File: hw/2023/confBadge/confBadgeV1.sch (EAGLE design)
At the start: 86 parts, among them J3 TYPE-C-31-M-12, Q1 8/16/20MHz, U1 ATMEGA328, U10 WS2812-2020, U11 WS2812-2020, U12 WS2812-2020, U13 WS2812-2020, U14 WS2812-2020, U15 WS2812-2020, U16 WS2812-2020, U17 WS2812-2020, U18 WS2812-2020, U19 WS2812-2020, U2 AP2112-3.3, U20 WS2812-2020, U21 WS2812-2020, U22 WS2812-2020, U3 WS2812-2020, U4 WS2812-2020, U5 PCM12SMTRPCM12SMTR_CNK, U6 24792479PCB_37P49X52P63_KEY, U7 CH340C, U8 SMF05CT1G, U9 WS2812-2020

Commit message: Updated schematic and layout for Conf-Badge
- adjusted for ATmega328PB
- change to USB-c
- switch sao and isp header to SMD
- moved sync-in and sync-out header for fit
- updated silkscreen for oled position
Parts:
- removed SV4: SAO, con-lstb:MA03-2
- removed SV5: ICSP, con-lstb:MA03-2
- added J1, J2: SSW-103-22-F-D-VS-K-TRCON3_SSW-D-DUMZ_HDR_SAI, SSW-103-22-F-D-VS-K-TR:SSW-103-22-F-D-VS-K-TRCON3_SSW-D-DUMZ_HDR_SAI
- added R16, R17, R18, R19, R8, R9: 10K, SparkFun:RESISTOR0603-RES
- added TP1, TP2: TPB1,27, testpad:TPB1,27
- R13, R14: value 1K -> 5.1K
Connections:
- new net PE0: TP2.TP, U1.GND@1
- new net PE1: TP1.TP, U1.VCC@2
- net 3.3V: now also J1.6, J2.1, R16.2, R17.2, R18.2, R19.2, R8.2, R9.2; no longer SV4.2, SV5.2, U1.VCC@2
- net BTN_A: now also R19.1
- net BTN_B: now also R18.1
- net BTN_D: now also R9.1
- net BTN_L: now also R8.1
- net BTN_R: now also R17.1
- net BTN_U: now also R16.1
- net DBG_LED: now also J1.3; no longer SV5.3
- net GND: now also J1.2, J2.2; no longer SV4.1, SV5.6, U1.GND@1
- net RESET: now also J1.1; no longer SV5.5
- net SAO_IO1: now also J1.4, J2.5; no longer SV4.6, SV5.4
- net SAO_IO2: now also J1.5, J2.6; no longer SV4.5, SV5.1
- net SCL: now also J2.4; no longer SV4.3
- net SDA: now also J2.3; no longer SV4.4
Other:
- note added: "8MHZ"
- note added: "Digikey: 2057-PH1RB-05-UA-ND Manuf: PH1RB-05-UA"
- note added: "Digikey: S5441-ND Manuf: PPTC051LGBN"
- note added: "ISP CONNECTOR"
- note added: "RESET GND SCK MOSI MISO 3V3"
- note added: "SAO CONNECTOR"
- note added: "Switch to Atmega328PB (for UID)"
- note removed: "MISO SCK RESET"
- note removed: "VCC MOSI GND"
- moved on the sheet: C1, C2, D2, Q1, R2, R6, S1, U1

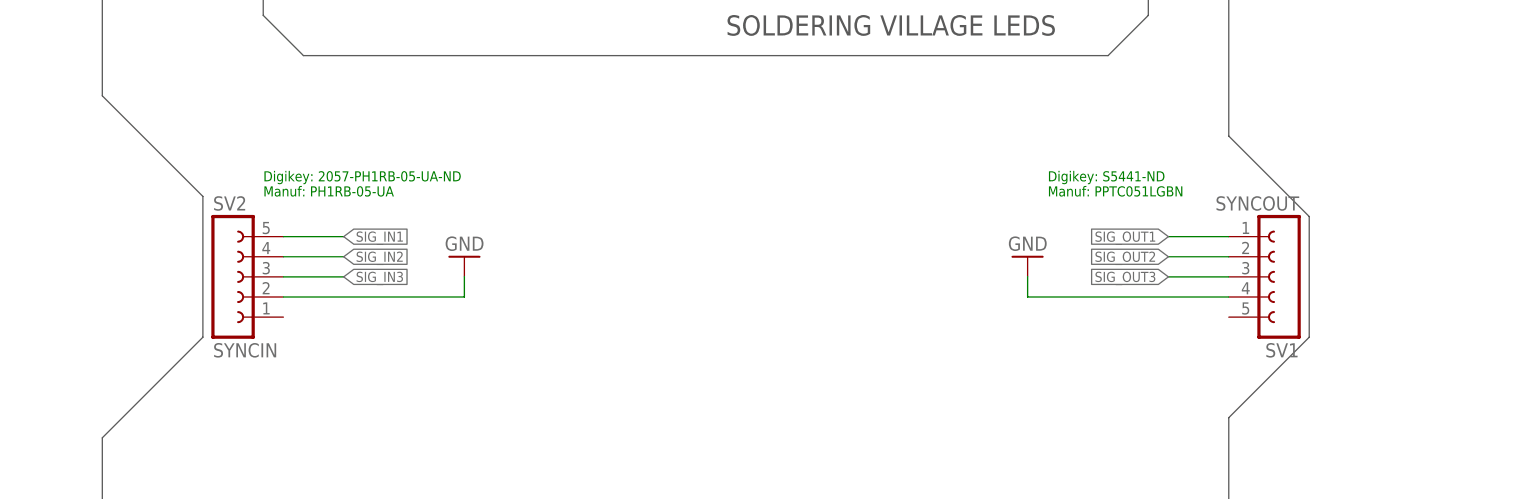
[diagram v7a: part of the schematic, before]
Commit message: added bottom pick-place file for rizome quote
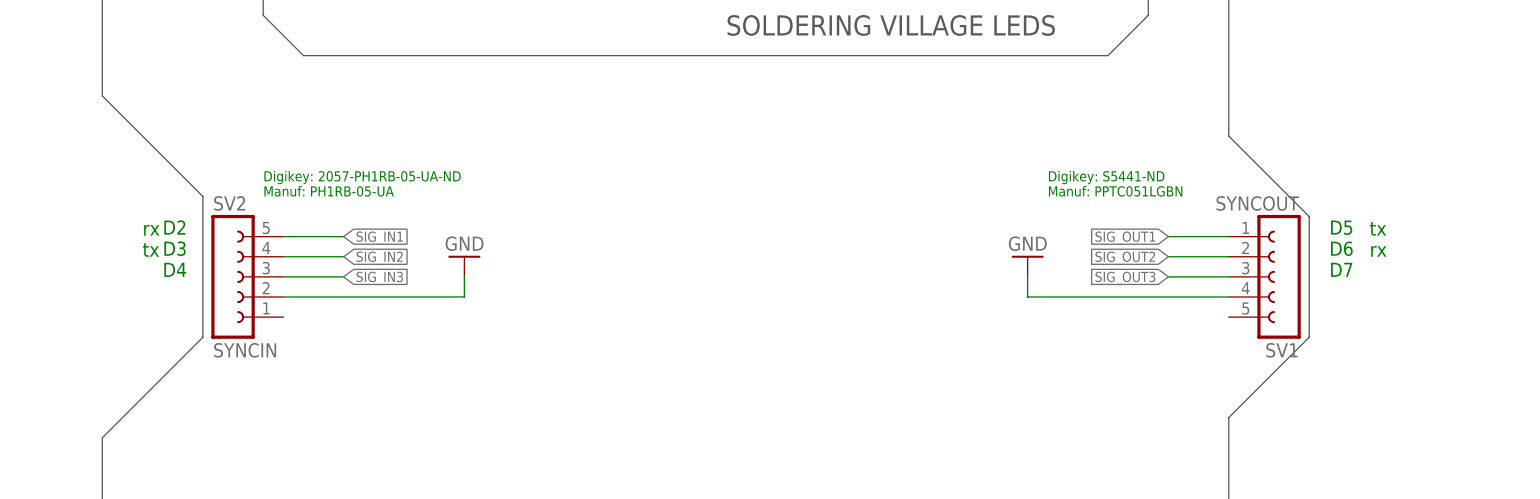
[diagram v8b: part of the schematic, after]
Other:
- note added: "D2 D3 D4"
- note added: "D5 D6 D7"
- note added: "rx tx"
- note added: "tx rx"
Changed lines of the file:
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@@
 (for UID)</text>
 <text x="81.28" y="83.82" size="2.54" layer="91">8MHZ</text>
+<text x="584.2" y="86.36" size="1.778" layer="91">D2
+D3
+D4</text>
+<text x="731.52" y="86.36" size="1.778" layer="91">D5
+D6
+D7</text>
+<text x="581.66" y="88.9" size="1.778" layer="91">rx
+tx</text>
+<text x="736.6" y="88.9" size="1.778" layer="91">tx
+rx</text>
 </plain>
 <instances>
